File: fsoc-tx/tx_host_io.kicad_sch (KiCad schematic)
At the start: 3 parts, among them J5 Conn_01x03

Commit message: TX: fixing unassigned footprints
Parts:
- R12, R13: footprint (none) -> Resistor_SMD:R_0603_1608Metric
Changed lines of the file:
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@@
 			)
 		)
-		(property "Footprint" ""
+		(property "Footprint" "Resistor_SMD:R_0603_1608Metric"
 			(at 111.252 90.17 90)
 			(hide yes)
@@
 			)
 		)
-		(property "Footprint" ""
+		(property "Footprint" "Resistor_SMD:R_0603_1608Metric"
 			(at 123.952 90.17 90)
 			(hide yes)

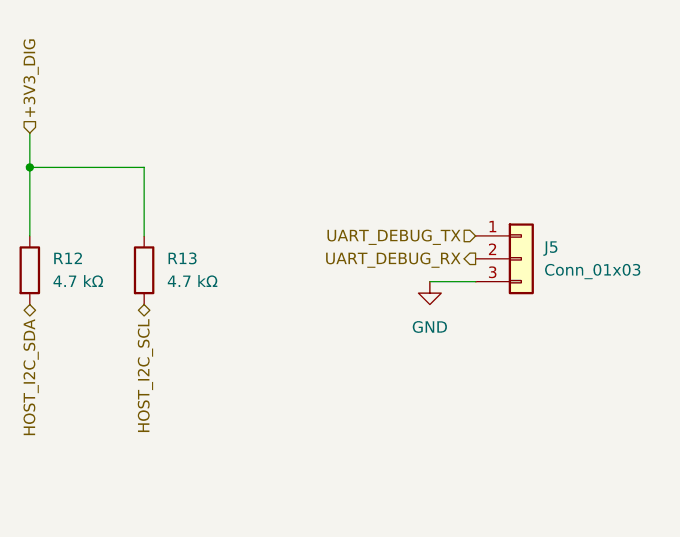
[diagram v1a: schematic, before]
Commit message: Switching ASTX-H11 to SiT5346 and SiT5346 datasheet
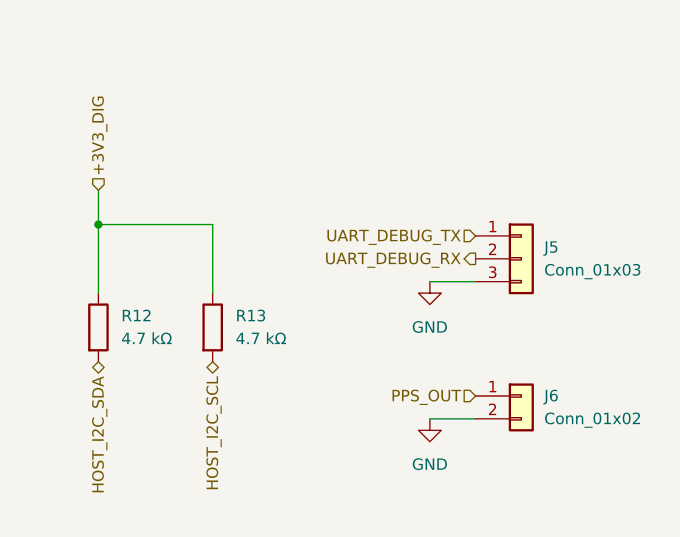
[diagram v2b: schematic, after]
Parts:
- added J6: Conn_01x02, Connector_PinHeader_2.54mm:PinHeader_1x02_P2.54mm_Vertical, symbol Connector_Generic:Conn_01x02
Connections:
- net GND: now also J6.2 (Pin_2)
- new net PPS_OUT: J6.1 (Pin_1)
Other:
- moved on the sheet: R12, R13
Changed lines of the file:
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@@
 	(paper "A4")
 	(junction
-		(at 113.03 78.74)
+		(at 120.65 85.09)
 		(diameter 0)
 		(color 0 0 0 0)
@@
 	(wire
 		(pts
-			(xy 125.73 86.36) (xy 125.73 78.74)
+			(xy 133.35 92.71) (xy 133.35 85.09)
 		)
 		(stroke
@@
 	(wire
 		(pts
-			(xy 125.73 78.74) (xy 113.03 78.74)
+			(xy 133.35 85.09) (xy 120.65 85.09)
 		)
 		(stroke
@@
 	(wire
 		(pts
-			(xy 113.03 78.74) (xy 113.03 86.36)
+			(xy 120.65 85.09) (xy 120.65 92.71)
 		)
 		(stroke
@@
 	(wire
 		(pts
-			(xy 157.48 91.44) (xy 162.56 91.44)
+			(xy 157.48 106.68) (xy 162.56 106.68)
 		)
 		(stroke
@@
 	(wire
 		(pts
-			(xy 113.03 74.93) (xy 113.03 78.74)
+			(xy 157.48 91.44) (xy 162.56 91.44)
 		)
 		(stroke
@@
 		)
 	)
+	(wire
+		(pts
+			(xy 120.65 81.28) (xy 120.65 85.09)
+		)
+		(stroke
+			(width 0)
+			(type default)
+		)
+	)
+	(hierarchical_label "PPS_OUT"
+		(shape input)
+		(at 162.56 104.14 180)
+		(effects
+			(font
+				(size 1.27 1.27)
+			)
+			(justify right)
+		)
+	)
 	(hierarchical_label "+3V3_DIG"
 		(shape input)
-		(at 113.03 74.93 90)
+		(at 120.65 81.28 90)
 		(effects
 			(font
@@
 	(hierarchical_label "HOST_I2C_SCL"
 		(shape bidirectional)
-		(at 125.73 93.98 270)
+		(at 133.35 100.33 270)
 		(effects
 			(font
@@
 	(hierarchical_label "HOST_I2C_SDA"
 		(shape bidirectional)
-		(at 113.03 93.98 270)
+		(at 120.65 100.33 270)
 		(effects
 			(font
@@
 	(symbol
 		(lib_id "Device:R")
-		(at 113.03 90.17 0)
+		(at 120.65 96.52 0)
 		(unit 1)
 		(body_style 1)
@@
 		(fields_autoplaced yes)
 		(property "Reference" "R12"
-			(at 115.57 88.8999 0)
+			(at 123.19 95.2499 0)
 			(show_name no)
 			(do_not_autoplace no)
@@
 		)
 		(property "Value" "4.7 kΩ"
-			(at 115.57 91.4399 0)
+			(at 123.19 97.7899 0)
 			(show_name no)
 			(do_not_autoplace no)
@@
 		)
 		(property "Footprint" "Resistor_SMD:R_0603_1608Metric"
-			(at 111.252 90.17 90)
+			(at 118.872 96.52 90)
 			(hide yes)
 			(show_name no)
@@
 		)
 		(property "Datasheet" ""
-			(at 113.03 90.17 0)
+			(at 120.65 96.52 0)
 			(hide yes)
 			(show_name no)
@@
 		)
 		(property "Description" "Resistor"
-			(at 113.03 90.17 0)
+			(at 120.65 96.52 0)
 			(hide yes)
 			(show_name no)
@@
 	(symbol
 		(lib_id "Device:R")
-		(at 125.73 90.17 0)
+		(at 133.35 96.52 0)
 		(unit 1)
 		(body_style 1)
@@
 		(fields_autoplaced yes)
 		(property "Reference" "R13"
-			(at 128.27 88.8999 0)
+			(at 135.89 95.2499 0)
 			(show_name no)
 			(do_not_autoplace no)
@@
 		)
 		(property "Value" "4.7 kΩ"
-			(at 128.27 91.4399 0)
+			(at 135.89 97.7899 0)
 			(show_name no)
 			(do_not_autoplace no)
@@
 		)
 		(property "Footprint" "Resistor_SMD:R_0603_1608Metric"
-			(at 123.952 90.17 90)
+			(at 131.572 96.52 90)
 			(hide yes)
 			(show_name no)
@@
 		)
 		(property "Datasheet" ""
-			(at 125.73 90.17 0)
+			(at 133.35 96.52 0)
 			(hide yes)
 			(show_name no)
@@
 		)
 		(property "Description" "Resistor"
-			(at 125.73 90.17 0)
+			(at 133.35 96.52 0)
 			(hide yes)
 			(show_name no)
@@
 				(path "/d92cb11a-a3ee-43a3-bd30-881774176ced/de1ed7cc-4a66-440d-ba62-c10288bf4fb2"
 					(reference "R13")
+					(unit 1)
+				)
+			)
+		)
+	)
+	(symbol
+		(lib_id "Connector_Generic:Conn_01x02")
+		(at 167.64 104.14 0)
+		(unit 1)
+		(body_style 1)
+		(exclude_from_sim no)
+		(in_bom yes)
+		(on_board yes)
+		(in_pos_files yes)
+		(dnp no)
+		(fields_autoplaced yes)
+		(property "Reference" "J6"
+			(at 170.18 104.1399 0)
+			(show_name no)
+			(do_not_autoplace no)
+			(effects
+				(font
+					(size 1.27 1.27)
+				)
+				(justify left)
+			)
+		)
+		(property "Value" "Conn_01x02"
+			(at 170.18 106.6799 0)
+			(show_name no)
+			(do_not_autoplace no)
+			(effects
+				(font
+					(size 1.27 1.27)
+				)
+				(justify left)
+			)
+		)
+		(property "Footprint" "Connector_PinHeader_2.54mm:PinHeader_1x02_P2.54mm_Vertical"
+			(at 167.64 104.14 0)
+			(hide yes)
+			(show_name no)
+			(do_not_autoplace no)
+			(effects
+				(font
+					(size 1.27 1.27)
+				)
+			)
+		)
+		(property "Datasheet" ""
+			(at 167.64 104.14 0)
+			(hide yes)
+			(show_name no)
+			(do_not_autoplace no)
+			(effects
+				(font
+					(size 1.27 1.27)
+				)
+			)
+		)
+		(property "Description" "Generic connector, single row, 01x02, script generated (kicad-library-utils/schlib/autogen/connector/)"
+			(at 167.64 104.14 0)
+			(hide yes)
+			(show_name no)
+			(do_not_autoplace no)
+			(effects
+				(font
+					(size 1.27 1.27)
+				)
+			)
+		)
+		(pin "1"
+		)
+		(pin "2"
+		)
+		(instances
+			(project "fsoc-tx"
+				(path "/d92cb11a-a3ee-43a3-bd30-881774176ced/de1ed7cc-4a66-440d-ba62-c10288bf4fb2"
+					(reference "J6")
 					(unit 1)
 				)
@@
 					(unit 1)
 				)
+			)
+		)
+	)
+	(symbol
+		(lib_id "power:GND")
+		(at 157.48 106.68 0)
+		(unit 1)
+		(body_style 1)
+		(exclude_from_sim no)
+		(in_bom yes)
+		(on_board yes)
+		(in_pos_files yes)
+		(dnp no)
+		(fields_autoplaced yes)
+		(property "Reference" "#PWR047"
+			(at 157.48 113.03 0)
+			(hide yes)
+			(show_name no)
+			(do_not_autoplace no)
+			(effects
+				(font
+					(size 1.27 1.27)
+				)
+			)
+		)
+		(property "Value" "GND"
+			(at 157.48 111.76 0)
+			(show_name no)
+			(do_not_autoplace no)
+			(effects
+				(font
+					(size 1.27 1.27)
+				)
+			)
+		)
+		(property "Footprint" ""
+			(at 157.48 106.68 0)
+			(hide yes)
+			(show_name no)
+			(do_not_autoplace no)
+			(effects
+				(font
+					(size 1.27 1.27)
+				)
+			)
+		)
+		(property "Datasheet" ""
+			(at 157.48 106.68 0)
+			(hide yes)
+			(show_name no)
+			(do_not_autoplace no)
+			(effects
+				(font
+					(size 1.27 1.27)
+				)
+			)
+		)
+		(property "Description" "Power symbol creates a global label with name \"GND\" , ground"
+			(at 157.48 106.68 0)
+			(hide yes)
+			(show_name no)
+			(do_not_autoplace no)
+			(effects
+				(font
+					(size 1.27 1.27)
+				)
+			)
+		)
+		(pin "1"
+		)
+		(instances
+			(project "fsoc-tx"
+				(path "/d92cb11a-a3ee-43a3-bd30-881774176ced/de1ed7cc-4a66-440d-ba62-c10288bf4fb2"
+					(reference "#PWR047")
+					(unit 1)
+				)
